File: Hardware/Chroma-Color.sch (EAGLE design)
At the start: 92 parts, among them J1 15-91-1102, J2 87832-6422, J3 1775470-6, J4 D2514-6V0C-AR-WD, J7 26-64-4040, U1 EP4CE6E22C8N, U2 ADP3338AKCZ-3.3-RL, U3 ADP3338AKCZ-2.5-RL, U4 NCV565ST12T3G, U5 M25P40-VMN6TPBCT, X1 ASDMB-50.000MHZ-LC-T

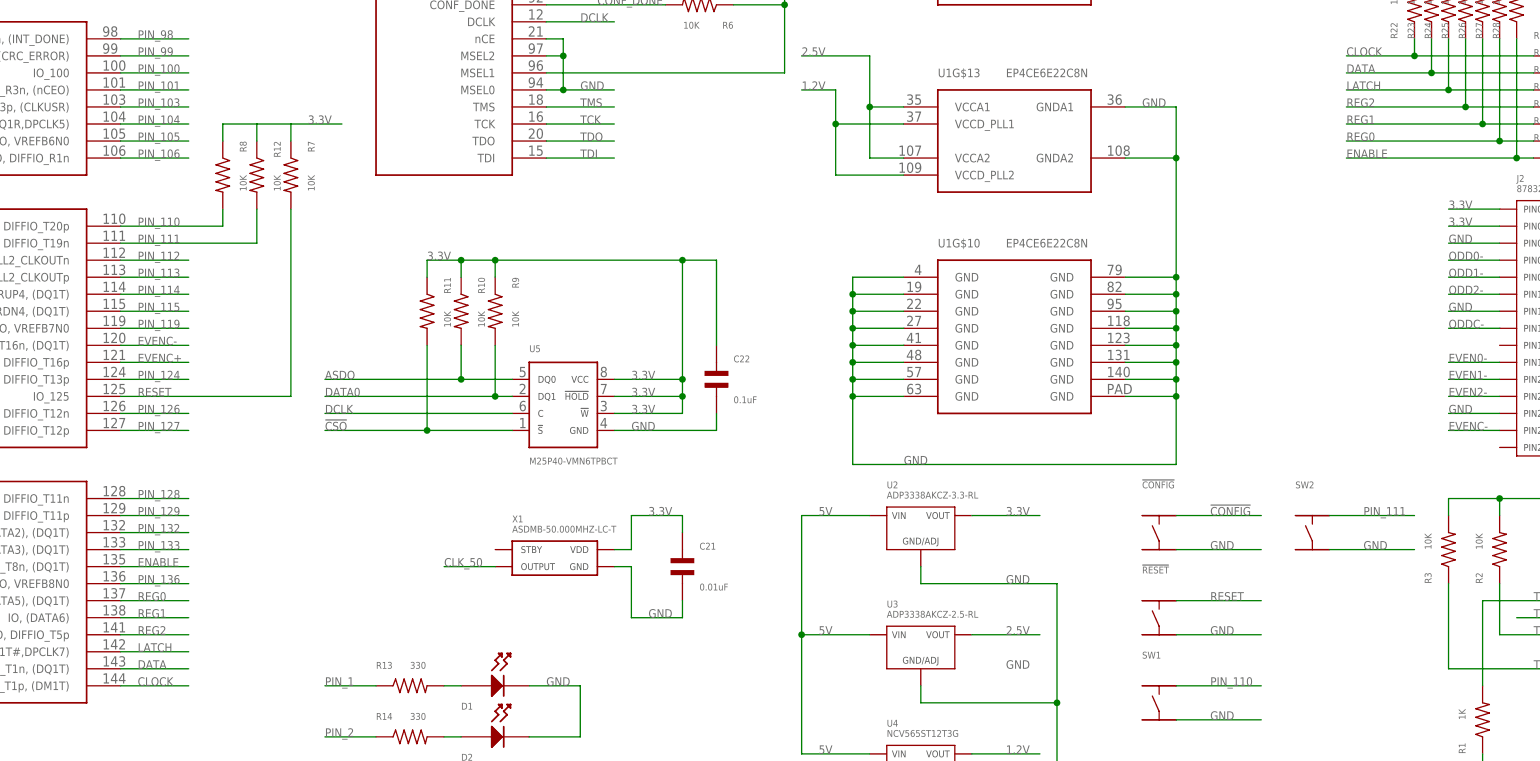
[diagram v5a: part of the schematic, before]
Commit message: Added SW3. Need to add a buffer/level shifter.
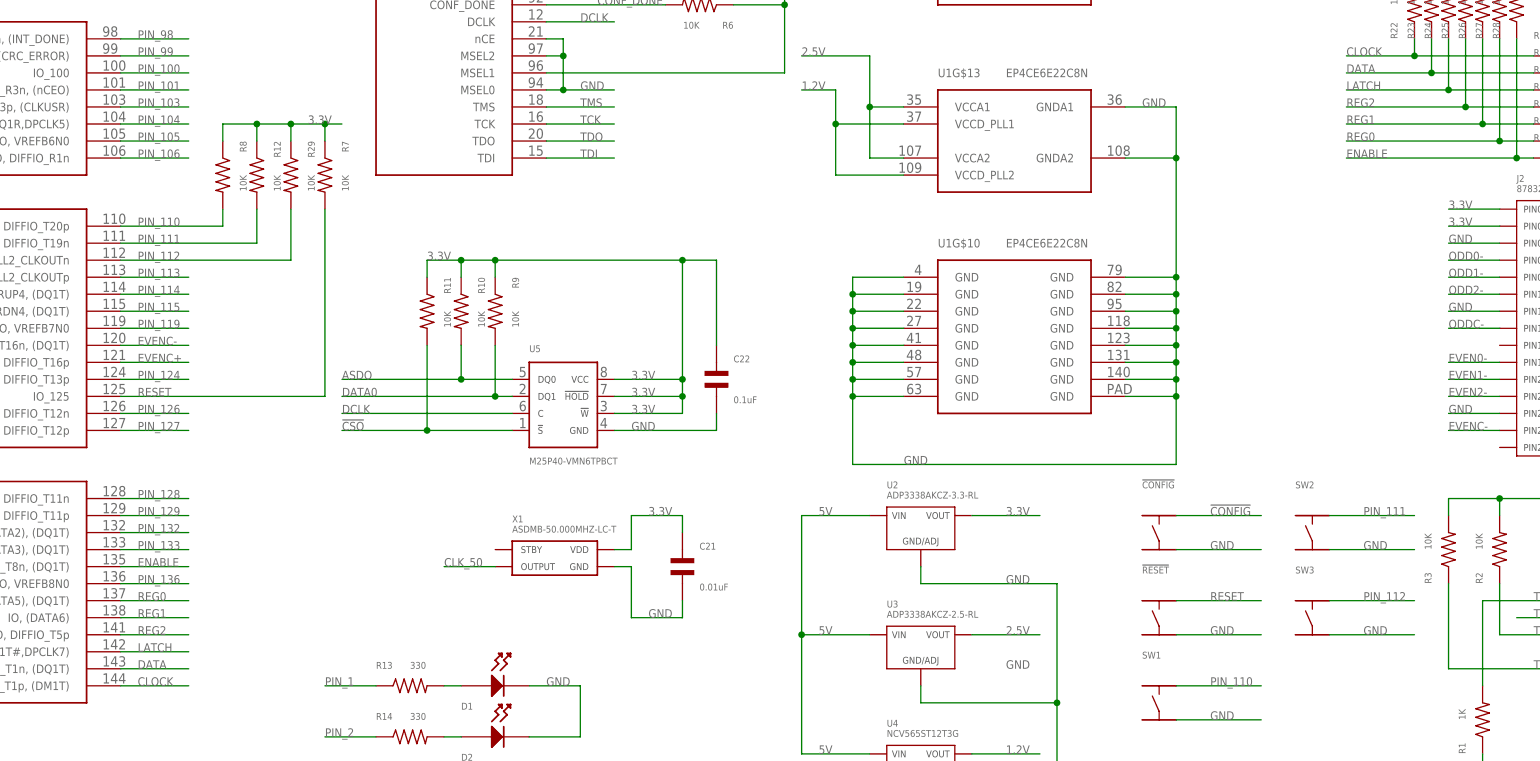
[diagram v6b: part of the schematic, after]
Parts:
- added R29: 10K, MF_Passives:RESISTOR_0603
- added SW3: (no value), MF_Switches:TACT_4.2MM
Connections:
- net 3.3V: now also R29.P$1
- net GND: now also SW3.P$4
- net PIN_112: now also R29.P$2, SW3.P$2
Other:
- moved on the sheet: R7
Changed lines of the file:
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@@
 </part>
 <part name="J3" library="PP_Connectors" deviceset="CON_01X06" device="_1775470-6" value="1775470-6"/>
+<part name="SW3" library="MF_Switches" deviceset="TACT" device="_4.2MM"/>
+<part name="R29" library="MF_Passives" deviceset="RESISTOR" device="_0603" value="10K"/>
 </parts>
 <sheets>
@@
 <instance part="!CONFIG" gate="G$1" x="-116.84" y="76.2"/>
 <instance part="!RESET" gate="G$1" x="-116.84" y="63.5"/>
-<instance part="R7" gate="G$1" x="-246.38" y="129.54" rot="R270"/>
+<instance part="R7" gate="G$1" x="-241.3" y="129.54" rot="R270"/>
 <instance part="J4" gate="G$1" x="-45.72" y="147.32"/>
 <instance part="C10" gate="G$1" x="-233.68" y="17.78"/>
@@
 <instance part="J7" gate="G$1" x="-111.76" y="35.56"/>
 <instance part="J3" gate="G$1" x="-27.94" y="167.64"/>
+<instance part="SW3" gate="G$1" x="-93.98" y="63.5"/>
+<instance part="R29" gate="G$1" x="-246.38" y="129.54" rot="R270"/>
 </instances>
 <busses>
@@
 <junction x="-66.04" y="162.56"/>
 </segment>
+<segment>
+<pinref part="SW3" gate="G$1" pin="P$4"/>
+<wire x1="-91.44" y1="60.96" x2="-78.74" y2="60.96" width="0.1524" layer="91"/>
+<label x="-86.36" y="60.96" size="1.27" layer="95" font="vector"/>
+</segment>
 </net>
 <net name="2.5V" class="0">
@@
 <segment>
 <pinref part="R7" gate="G$1" pin="P$1"/>
-<wire x1="-246.38" y1="134.62" x2="-246.38" y2="137.16" width="0.1524" layer="91"/>
-<wire x1="-246.38" y1="137.16" x2="-238.76" y2="137.16" width="0.1524" layer="91"/>
+<wire x1="-241.3" y1="134.62" x2="-241.3" y2="137.16" width="0.1524" layer="91"/>
+<wire x1="-241.3" y1="137.16" x2="-238.76" y2="137.16" width="0.1524" layer="91"/>
 <label x="-243.84" y="137.16" size="1.27" layer="95" font="vector"/>
 <pinref part="R8" gate="G$1" pin="P$1"/>
+<wire x1="-241.3" y1="137.16" x2="-246.38" y2="137.16" width="0.1524" layer="91"/>
 <wire x1="-246.38" y1="137.16" x2="-251.46" y2="137.16" width="0.1524" layer="91"/>
 <wire x1="-251.46" y1="137.16" x2="-256.54" y2="137.16" width="0.1524" layer="91"/>
@@
 <pinref part="R12" gate="G$1" pin="P$1"/>
 <wire x1="-251.46" y1="134.62" x2="-251.46" y2="137.16" width="0.1524" layer="91"/>
+<pinref part="R29" gate="G$1" pin="P$1"/>
+<wire x1="-246.38" y1="134.62" x2="-246.38" y2="137.16" width="0.1524" layer="91"/>
+<junction x="-251.46" y="137.16"/>
+<junction x="-246.38" y="137.16"/>
+<junction x="-241.3" y="137.16"/>
 </segment>
 <segment>
@@
 <segment>
 <pinref part="U1" gate="G$7" pin="125"/>
-<wire x1="-271.78" y1="96.52" x2="-246.38" y2="96.52" width="0.1524" layer="91"/>
+<wire x1="-271.78" y1="96.52" x2="-241.3" y2="96.52" width="0.1524" layer="91"/>
 <label x="-269.24" y="96.52" size="1.27" layer="95" font="vector"/>
 <pinref part="R7" gate="G$1" pin="P$2"/>
-<wire x1="-246.38" y1="96.52" x2="-246.38" y2="124.46" width="0.1524" layer="91"/>
+<wire x1="-241.3" y1="96.52" x2="-241.3" y2="124.46" width="0.1524" layer="91"/>
 </segment>
 <segment>
@@
 <segment>
 <pinref part="U1" gate="G$7" pin="112"/>
-<wire x1="-271.78" y1="116.84" x2="-261.62" y2="116.84" width="0.1524" layer="91"/>
 <label x="-269.24" y="116.84" size="1.27" layer="95" font="vector"/>
+<pinref part="R29" gate="G$1" pin="P$2"/>
+<wire x1="-271.78" y1="116.84" x2="-246.38" y2="116.84" width="0.1524" layer="91"/>
+<wire x1="-246.38" y1="116.84" x2="-246.38" y2="124.46" width="0.1524" layer="91"/>
+</segment>
+<segment>
+<pinref part="SW3" gate="G$1" pin="P$2"/>
+<wire x1="-91.44" y1="66.04" x2="-78.74" y2="66.04" width="0.1524" layer="91"/>
+<label x="-86.36" y="66.04" size="1.27" layer="95" font="vector"/>
 </segment>
 </net>
@@
 <wire x1="-213.36" y1="91.44" x2="-226.06" y2="91.44" width="0.1524" layer="91"/>
 <pinref part="R11" gate="G$1" pin="P$2"/>
-<wire x1="-226.06" y1="91.44" x2="-241.3" y2="91.44" width="0.1524" layer="91"/>
+<wire x1="-226.06" y1="91.44" x2="-238.76" y2="91.44" width="0.1524" layer="91"/>
 <wire x1="-226.06" y1="104.14" x2="-226.06" y2="91.44" width="0.1524" layer="91"/>
 <junction x="-226.06" y="91.44"/>
-<label x="-241.3" y="91.44" size="1.27" layer="95" font="vector"/>
+<label x="-238.76" y="91.44" size="1.27" layer="95" font="vector"/>
 </segment>
 <segment>
@@
 <net name="DATA0" class="0">
 <segment>
-<label x="-241.3" y="96.52" size="1.27" layer="95" font="vector"/>
+<label x="-238.76" y="96.52" size="1.27" layer="95" font="vector"/>
 <pinref part="R9" gate="G$1" pin="P$2"/>
-<wire x1="-215.9" y1="96.52" x2="-241.3" y2="96.52" width="0.1524" layer="91"/>
+<wire x1="-215.9" y1="96.52" x2="-238.76" y2="96.52" width="0.1524" layer="91"/>
 <wire x1="-215.9" y1="104.14" x2="-215.9" y2="96.52" width="0.1524" layer="91"/>
 <junction x="-215.9" y="96.52"/>
@@
 <wire x1="-213.36" y1="99.06" x2="-220.98" y2="99.06" width="0.1524" layer="91"/>
 <pinref part="R10" gate="G$1" pin="P$2"/>
-<wire x1="-220.98" y1="99.06" x2="-241.3" y2="99.06" width="0.1524" layer="91"/>
+<wire x1="-220.98" y1="99.06" x2="-238.76" y2="99.06" width="0.1524" layer="91"/>
 <wire x1="-220.98" y1="104.14" x2="-220.98" y2="99.06" width="0.1524" layer="91"/>
-<label x="-241.3" y="99.06" size="1.27" layer="95" font="vector"/>
+<label x="-238.76" y="99.06" size="1.27" layer="95" font="vector"/>
 <junction x="-220.98" y="99.06"/>
 </segment>
@@
 <net name="DCLK" class="0">
 <segment>
-<wire x1="-241.3" y1="93.98" x2="-213.36" y2="93.98" width="0.1524" layer="91"/>
-<label x="-241.3" y="93.98" size="1.27" layer="95" font="vector"/>
+<wire x1="-238.76" y1="93.98" x2="-213.36" y2="93.98" width="0.1524" layer="91"/>
+<label x="-238.76" y="93.98" size="1.27" layer="95" font="vector"/>
 <pinref part="U5" gate="G$1" pin="C"/>
 </segment>

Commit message: Working on adding level shifter and LVDS 3 R
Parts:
- added C39: 0.1uF, MF_Passives:CAPACITOR_NP_0603
- added U6: SN74LVC8T245RHLR, PP_DigitalIC:SN74LVC8T245_RHL
- added VOLT_SW: (no value), MF_Connectors:HEADER_01X03_PTH_2.54MM
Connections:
- new net CLOCK_LS: U1G$8.144, U6.A1
- new net DATA_LS: U1G$8.143, U6.A2
- new net ENABLE_LS: U1G$8.135, U6.A7
- new net LATCH_LS: U1G$8.142, U6.A3
- new net REG0_LS: U1G$8.137, U6.A6
- new net REG1_LS: U1G$8.138, U6.A5
- new net REG2_LS: U1G$8.141, U6.A4
- new net VCCB: U6.VCCB, VOLT_SW.PIN1
- net 2.5V: now also C1.P$1, C27.P$1, C28.P$1, C3.P$1, C4.P$1, C5.P$1, C6.P$1, U1G$12.117, U1G$12.122, U1G$12.40, U1G$12.47, U1G$12.56, U1G$12.62, U1G$12.81
- net 3.3V: now also C39.P$1, U6.VCCA, VOLT_SW.PIN0; no longer C1.P$1, C27.P$1, C28.P$1, C3.P$1, C4.P$1, C5.P$1, C6.P$1, U1G$12.117, U1G$12.122, U1G$12.40, U1G$12.47, U1G$12.56, U1G$12.62, U1G$12.81
- net 5V: now also VOLT_SW.PIN2
- net CLOCK: now also U6.B1; no longer U1G$8.144
- net DATA: now also U6.B2; no longer U1G$8.143
- net ENABLE: now also U6.B7; no longer U1G$8.135
- net GND: now also C39.P$2, U6.!OE, U6.DIR, U6.GND
- net LATCH: now also U6.B3; no longer U1G$8.142
- net REG0: now also U6.B6; no longer U1G$8.137
- net REG1: now also U6.B5; no longer U1G$8.138
- net REG2: now also U6.B4; no longer U1G$8.141
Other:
- moved on the sheet: C1, C10, C12, C13, C17, C18, C2, C20, C23, C25, C26, C27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

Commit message: REV 2 done.
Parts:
- removed FID3: FIDUCIAL_0.5MM, MF_Aesthetics:FIDUCIAL_0.5MM
- added R30, R31, R33, R34, R36, R37, R39, R40, R42, R43, R45, R46, R48, R49, R51, R52: 120, MF_Passives:RESISTOR_0402
- added R32, R35, R38, R41, R44, R47, R50, R53: 170, MF_Passives:RESISTOR_0402
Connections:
- new net EVEN0+_RN: J2.PIN19, R42.P$2, R44.P$2
- new net EVEN0-_RN: J2.PIN18, R43.P$2, R44.P$1
- new net EVEN1+_RN: J2.PIN21, R45.P$2, R47.P$2
- new net EVEN1-_RN: J2.PIN20, R46.P$2, R47.P$1
- new net EVEN2+_RN: J2.PIN23, R48.P$2, R50.P$2
- new net EVEN2-_RN: J2.PIN22, R49.P$2, R50.P$1
- new net EVENC+_RN: J2.PIN27, R51.P$2, R53.P$2
- new net EVENC-_RN: J2.PIN26, R52.P$2, R53.P$1
- new net ODD0+_RN: J2.PIN7, R31.P$2, R32.P$2
- new net ODD0-_RN: J2.PIN6, R30.P$2, R32.P$1
- new net ODD1+_RN: J2.PIN9, R33.P$2, R35.P$2
- new net ODD1-_RN: J2.PIN8, R34.P$2, R35.P$1
- new net ODD2+_RN: J2.PIN11, R36.P$2, R38.P$2
- new net ODD2-_RN: J2.PIN10, R37.P$2, R38.P$1
- new net ODDC+_RN: J2.PIN15, R39.P$2, R41.P$2
- new net ODDC-_RN: J2.PIN14, R40.P$2, R41.P$1
- net 2.5V: now also R12.P$1, R29.P$1, R7.P$1, R8.P$1
- net 3.3V: no longer R12.P$1, R29.P$1, R7.P$1, R8.P$1
- net EVEN0+: now also R42.P$1; no longer J2.PIN19
- net EVEN0-: now also R43.P$1; no longer J2.PIN18
- net EVEN1+: now also R45.P$1; no longer J2.PIN21
- net EVEN1-: now also R46.P$1; no longer J2.PIN20
- net EVEN2+: now also R48.P$1; no longer J2.PIN23
- net EVEN2-: now also R49.P$1; no longer J2.PIN22
- net EVENC+: now also R51.P$1; no longer J2.PIN27
- net EVENC-: now also R52.P$1; no longer J2.PIN26
- net ODD0+: now also R31.P$1; no longer J2.PIN7
- net ODD0-: now also R30.P$1; no longer J2.PIN6
- net ODD1+: now also R33.P$1; no longer J2.PIN9
- net ODD1-: now also R34.P$1; no longer J2.PIN8
- net ODD2+: now also R36.P$1; no longer J2.PIN11
- net ODD2-: now also R37.P$1; no longer J2.PIN10
- net ODDC+: now also R39.P$1; no longer J2.PIN15
- net ODDC-: now also R40.P$1; no longer J2.PIN14
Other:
- moved on the sheet: C21, C22, C39, J1, J2, J3, J4, J5, J6, J7, R1, R10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
